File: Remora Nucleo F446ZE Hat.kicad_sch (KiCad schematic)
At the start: 20 parts, among them J1 NucleoF446ZE CN11 Header, J2 MSD-1-A, J3 UART_TX, J4 NucleoF446ZE CN12 Header, SW1 SW_Push

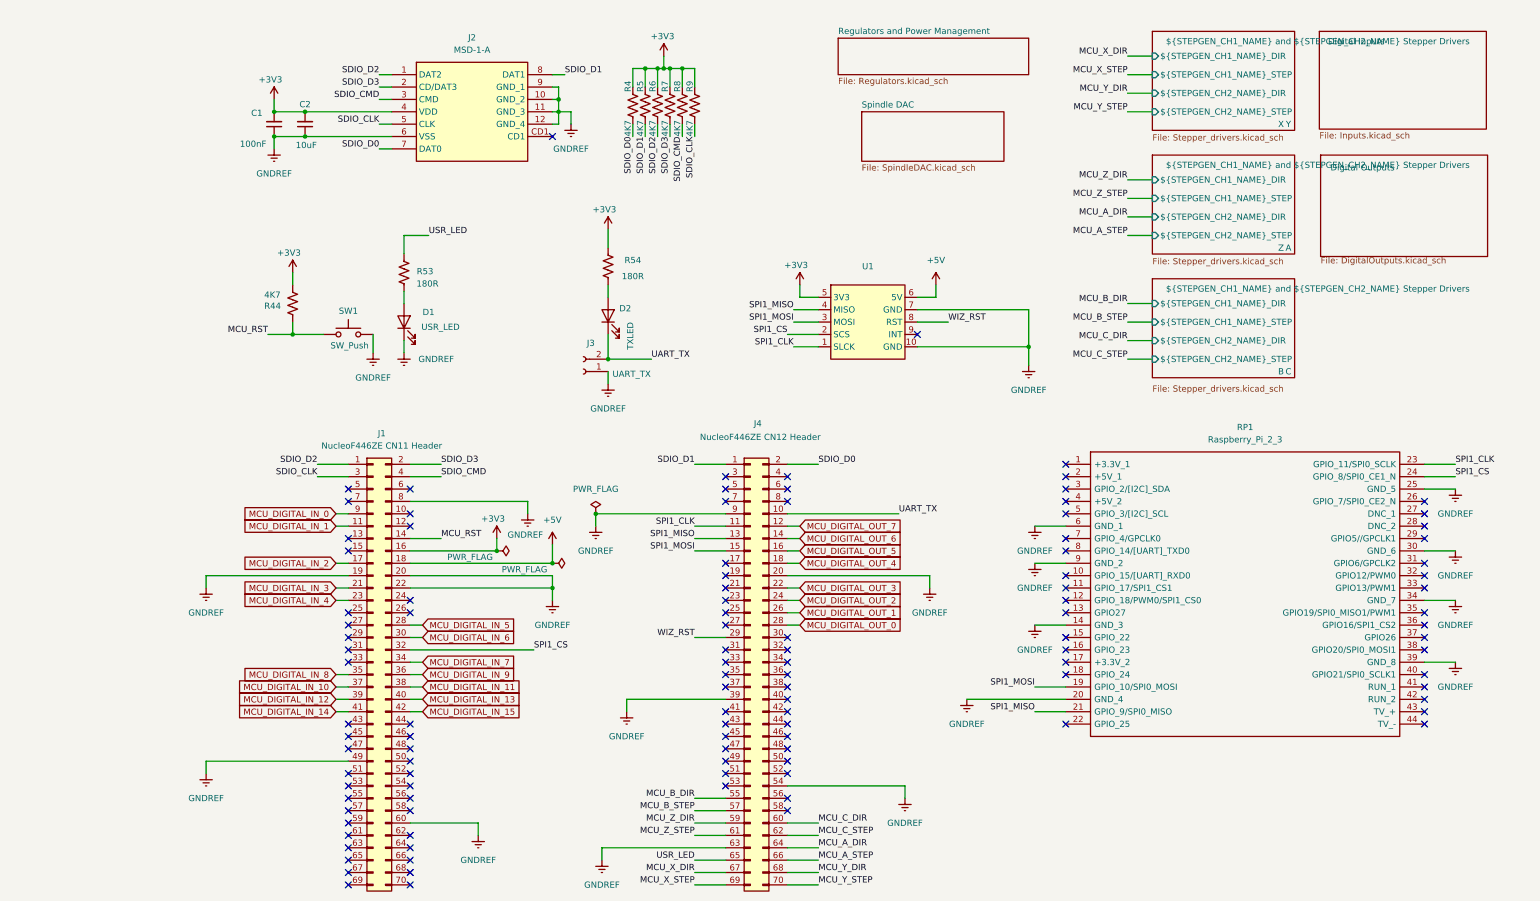
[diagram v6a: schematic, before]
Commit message: more BOM consolidation. Switched out IO for vertical toolless wire to board terminals and added footprints. Put new isolated ground plane on board.
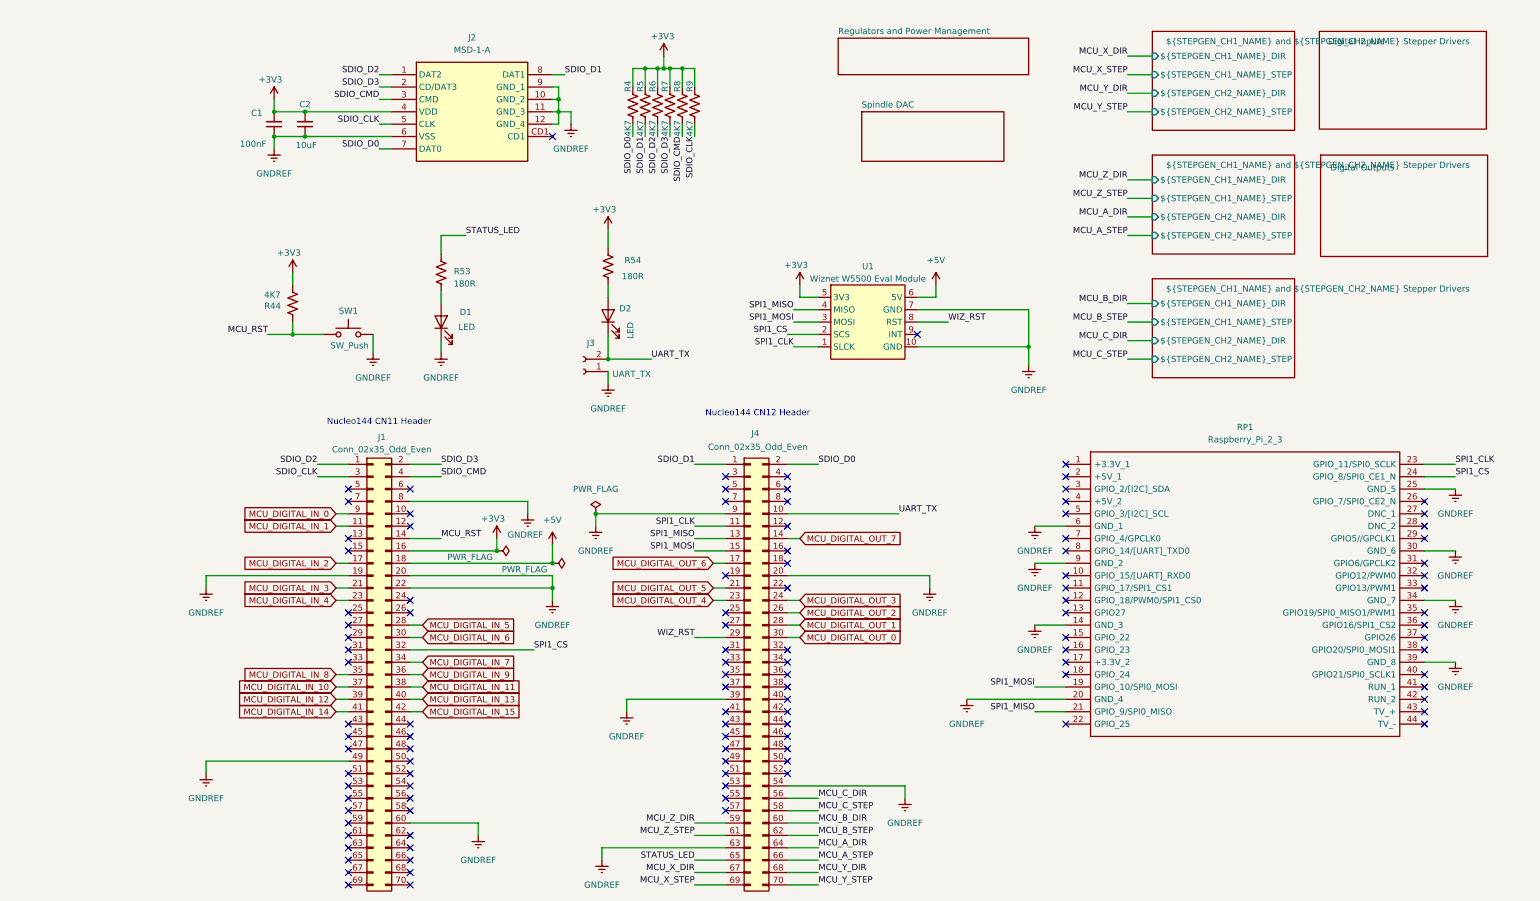
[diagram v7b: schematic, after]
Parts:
- D1: value USR_LED -> LED
- D2: value TXLED -> LED; Digikey Part Number 3147-B1501USD-20D000313U1930CT-ND -> 3147-B1501USD-20D000313U1930CT-ND
- J1: value NucleoF446ZE CN11 Header -> Conn_02x35_Odd_Even
- J4: value NucleoF446ZE CN12 Header -> Conn_02x35_Odd_Even; Digikey URL https://www.digikey.com.au/en/products/detail/samtec-inc/SSW-135-03-T-D/7886849 -> https://www.digikey.com.au/en/products/detail/samtec-inc/SSW-135-03-T-D/7886849
- RP1: Digikey Part Number SAM15594-ND -> SAM1204-20-ND; Digikey URL https://www.digikey.com.au/en/products/detail/samtec-inc/ES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 -> https://www.digikey.com.au/en/products/detail/samtec-inc/SS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
- U1: value ~ -> Wiznet W5500 Eval Module
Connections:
- net MCU_B_DIR: now also J4.60 (Pin_60); no longer J4.55 (Pin_55)
- net MCU_B_STEP: now also J4.62 (Pin_62); no longer J4.57 (Pin_57)
- net MCU_C_DIR: now also J4.56 (Pin_56); no longer J4.60 (Pin_60)
- net MCU_C_STEP: now also J4.58 (Pin_58); no longer J4.62 (Pin_62)
- net MCU_DIGITAL_OUT_0: now also J4.30 (Pin_30); no longer J4.28 (Pin_28)
- net MCU_DIGITAL_OUT_1: now also J4.28 (Pin_28); no longer J4.26 (Pin_26)
- net MCU_DIGITAL_OUT_2: now also J4.26 (Pin_26); no longer J4.24 (Pin_24)
- net MCU_DIGITAL_OUT_3: now also J4.24 (Pin_24); no longer J4.22 (Pin_22)
- net MCU_DIGITAL_OUT_4: now also J4.23 (Pin_23); no longer J4.18 (Pin_18)
- net MCU_DIGITAL_OUT_5: now also J4.21 (Pin_21); no longer J4.16 (Pin_16)
- net MCU_DIGITAL_OUT_6: now also J4.17 (Pin_17); no longer J4.14 (Pin_14)
- net MCU_DIGITAL_OUT_7: now also J4.14 (Pin_14); no longer J4.12 (Pin_12)
- net USR_LED renamed STATUS_LED
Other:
- note added: "Nucleo144 CN11 Header"
- note added: "Nucleo144 CN12 Header"
- moved on the sheet: D1, R53

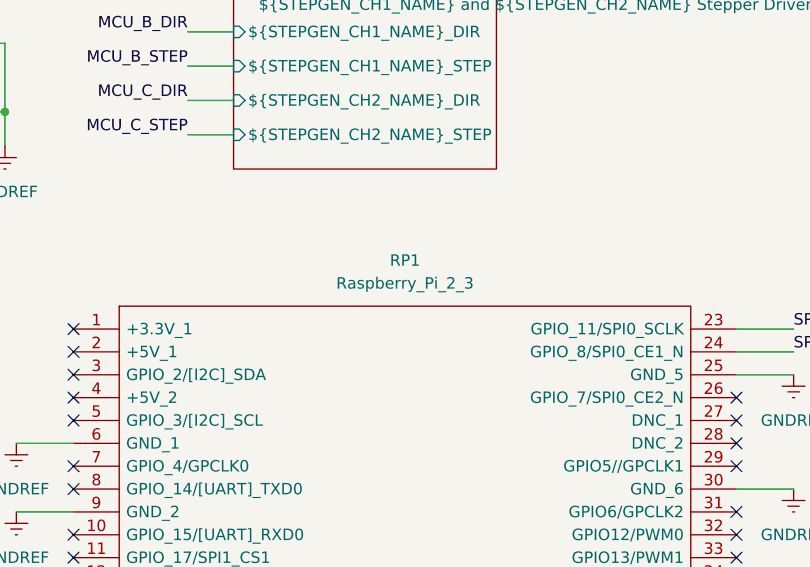
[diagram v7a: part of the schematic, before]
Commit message: Swapped out stepper isolators to use same as others. further BOM consolidation. Fixed bug with incorrect differential driver footprint.
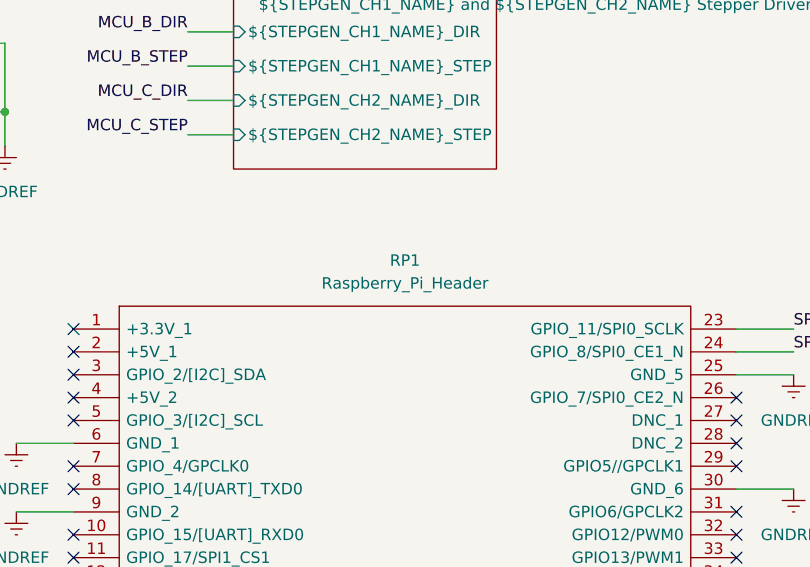
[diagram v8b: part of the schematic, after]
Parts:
- RP1: value Raspberry_Pi_2_3 -> Raspberry_Pi_Header
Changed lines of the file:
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@@
 			)
 		)
-		(property "Value" "Raspberry_Pi_2_3"
+		(property "Value" "Raspberry_Pi_Header"
 			(at 231.14 100.33 0)
 			(effects
